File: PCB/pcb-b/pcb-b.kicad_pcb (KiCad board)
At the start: 2 copper layers, 90.3 x 40 mm, 82 parts, among them J1 Conn_02x05_Counter_Clockwise, J2 Conn_02x05_Counter_Clockwise, K1 HK19F-DCxxV-SHC, Q1 BC817, Q10 BC817, Q11 TPCA8120,L1Q, Q13 TPCA8120,L1Q, Q14 BC817, Q15 BC817, Q19 BC817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

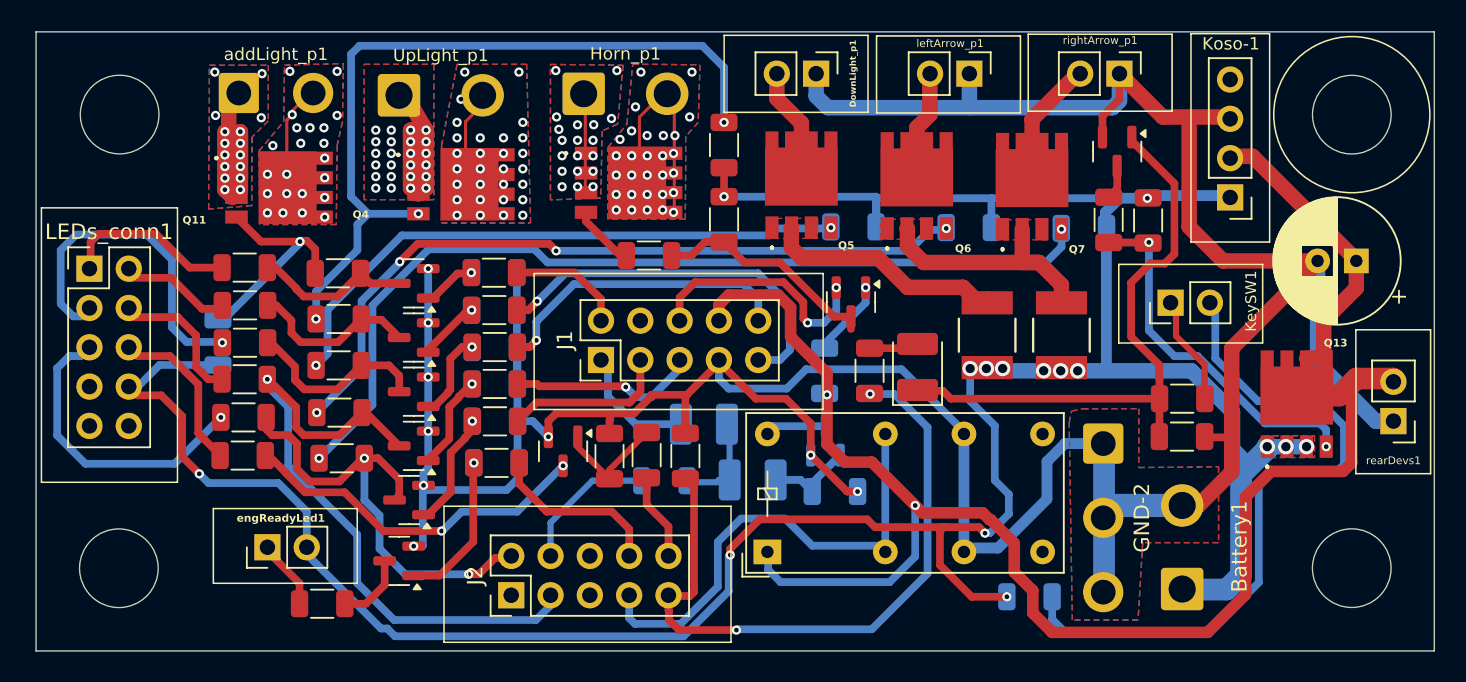
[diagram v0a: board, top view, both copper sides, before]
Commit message: PCB(b) size reduction and unuseful resistors removed
Originally, I placed resistors between the MOSFET's gate and the NPN collector to reduce the possible VGS voltage difference.
But, reading the TCPA8120's datasheet I have seen it accepts VGS max -20!! But in motorbike battey I never see 20 volts. So,
I removed the resistors. Now, when the NPN is conducing then the VGS will be about -12 volts, it is also better to avoid the
MOSFETs work in linear mode.

Thank to this component removing, also the PCB size has been reduced (85.6mm x 40.0mm). But, in order to get the size reduction
the add-light connector has been splitted in two single wite connectors. It is not beautiful to see, bet the PCB size is a too
big problem, and multilayer solution is a too expensive one!
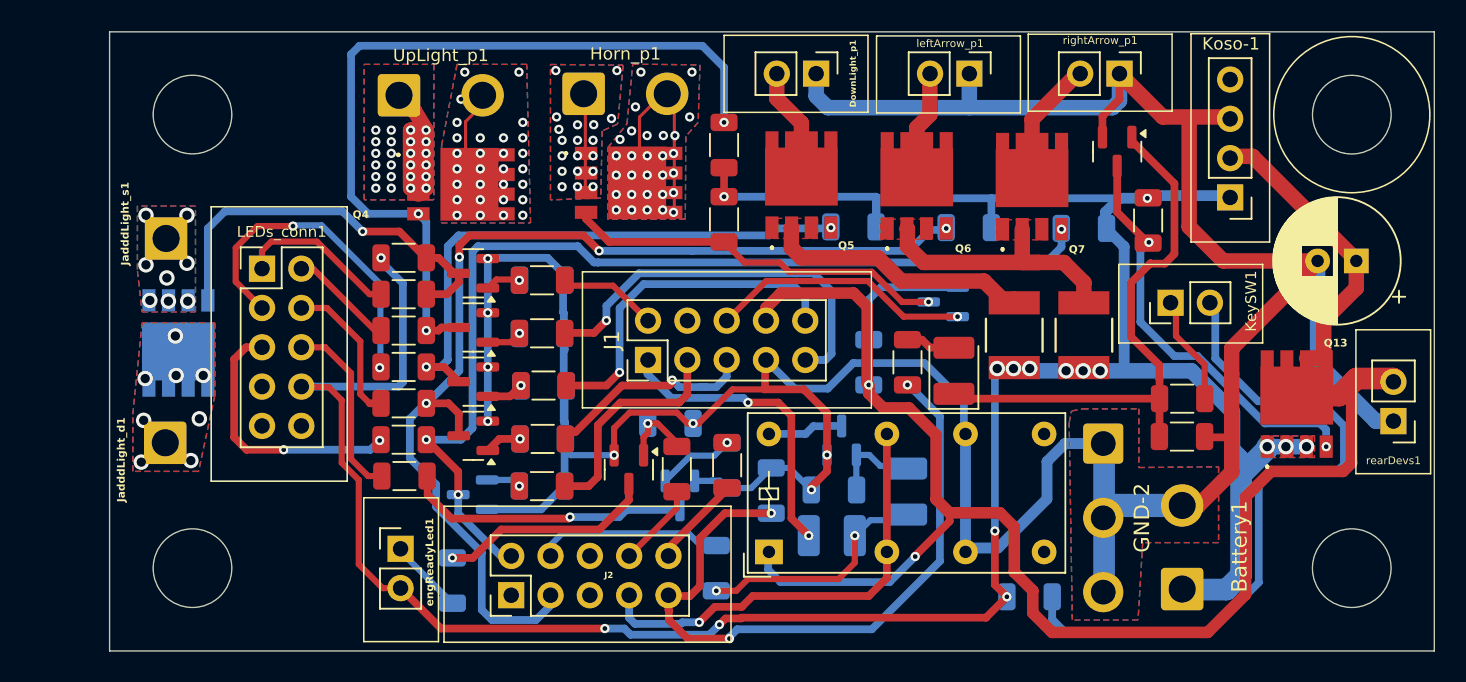
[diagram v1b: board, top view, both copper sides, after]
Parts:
- removed R3, RA10, RA11, RA12, RA13, RA14, RA7: 33K, Resistor_SMD:R_1206_3216Metric
- removed addLight_p1: Conn_01x02, Connector_Wire:SolderWire-0.75sqmm_1x02_P4.8mm_D1.25mm_OD2.3mm
- added JadddLight_d1: Conn_01x01, Connector_Wire:SolderWire-1sqmm_1x01_D1.4mm_OD2.7mm, F.Cu at (110.5, 96.5)
- added JadddLight_s1: Conn_01x01, Connector_Wire:SolderWire-1sqmm_1x01_D1.4mm_OD2.7mm, F.Cu at (110.5, 83.3)
- Q10, Q11, Q19, Q20, R6, RA39, RA9: moved to B.Cu
- R2, RA25, RA26, RA27, RA28: value 10K -> 15K
- RA24: value 10K -> 15K; moved to F.Cu
- RA42: value 10k -> 15k
- moved Q21 16.0 mm to (140.4, 98.3), turned to -90 degrees
- moved RA24 13.2 mm to (125.9, 84.6), turned to 0 degrees
- moved Q11 12.0 mm to (111.3, 90.1), turned to 0 degrees
- moved RA16 11.7 mm to (143.6, 98.2), turned to -90 degrees
- moved RA40 11.5 mm to (143.1, 95.3)
- moved LEDs_conn1 11.2 mm to (116.8, 85.3)
- moved D3 11.0 mm to (153.6, 102.5)
- moved RA6 10.5 mm to (126.0, 98.7)
- moved RA5 10.4 mm to (125.9, 96.3)
- moved RA1 10.4 mm to (125.9, 87.0)
- moved RA4 10.4 mm to (125.9, 94.0)
- moved RA2 10.4 mm to (125.9, 89.3)
- moved RA3 10.4 mm to (125.9, 91.7)
- moved D2 9.98 mm to (158.4, 99.7), turned to -90 degrees
- moved engReadyLed1 8.60 mm to (125.7, 103.4), turned to 0 degrees
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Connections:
- Q11 pad 4: Net-(Q11-G) -> Net-(Q1-C)
- Q4 pad 4: Net-(Q4-G) -> Net-(Q2-C)
- Q5 pad 4: Net-(Q5-G) -> Net-(Q14-C)
- Q6 pad 4: Net-(Q6-G) -> c_leftArrow
- Q7 pad 4: Net-(Q7-G) -> c_rightArrow
- Q8 pad 4: Net-(Q8-G) -> Net-(Q10-C)
- Q9 pad 3: Net-(Q9-C) -> Net-(Q13-G)
- RA24 pad 2: Net-(Q11-G) -> Net-(Q1-C)
- RA25 pad 2: Net-(Q4-G) -> Net-(Q2-C)
- RA26 pad 2: Net-(Q5-G) -> Net-(Q14-C)
- RA27 pad 2: Net-(Q6-G) -> c_leftArrow
- RA28 pad 2: Net-(Q7-G) -> c_rightArrow
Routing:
- net Net-(Q7-G): track 59.5 -> 0.00 mm, vias 2 -> 0
- net Net-(Q4-G): track 50.8 -> 0.00 mm, vias 3 -> 0
- net Net-(Q6-G): track 48.5 -> 0.00 mm, vias 4 -> 0
- net Net-(Q2-C): track 11.1 -> 52.4 mm, vias 0 -> 3
- net Net-(Q5-G): track 38.6 -> 0.00 mm, vias 2 -> 0
- net c_rightArrow: track 30.3 -> 65.4 mm, vias 2 -> 3
- net c_leftArrow: track 42.4 -> 69.2 mm, vias 1 -> 4
- net Net-(Q14-C): track 12.2 -> 36.7 mm, vias 0 -> 2
- net Net-(JadddLight_s1-Pin_1): track 16.7 -> 0.00 mm, vias 16 -> 8
- net Net-(Q1-C): track 10.2 -> 26.0 mm, vias 0 -> 1
- net Net-(Q11-G): track 15.0 -> 0.00 mm, vias 1 -> 0
- net i_powerOFF: track 7.99 -> 19.6 mm, vias 0 -> 2
- net Net-(Q10-C): track 14.7 -> 24.8 mm, vias 0 -> 1
- net Net-(Q21-C): track 4.63 -> 14.0 mm, vias 0 -> 1
- net Net-(D2-A): track 6.53 -> 15.4 mm, vias 0 -> 2
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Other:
- board size 90.3 x 40 mm -> 85.6 x 40 mm

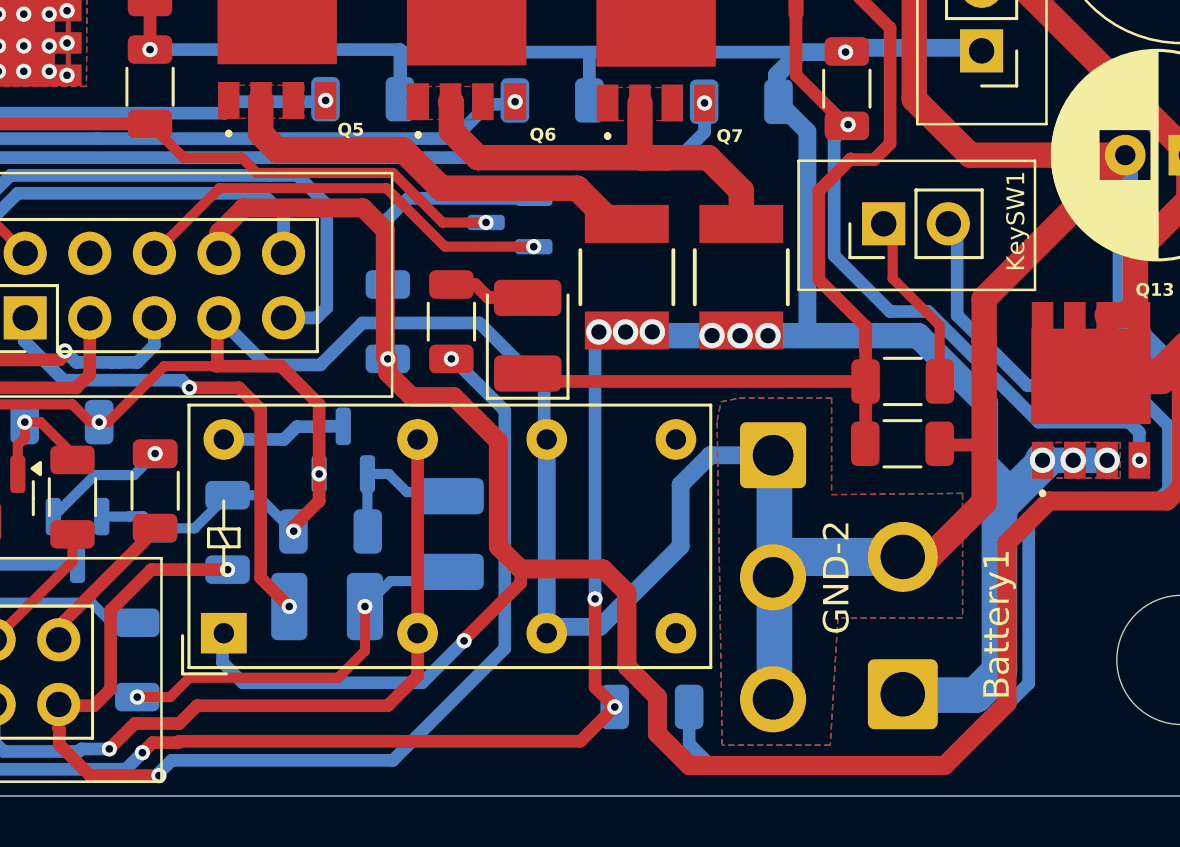
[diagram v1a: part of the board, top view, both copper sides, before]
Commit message: Flyback diode added
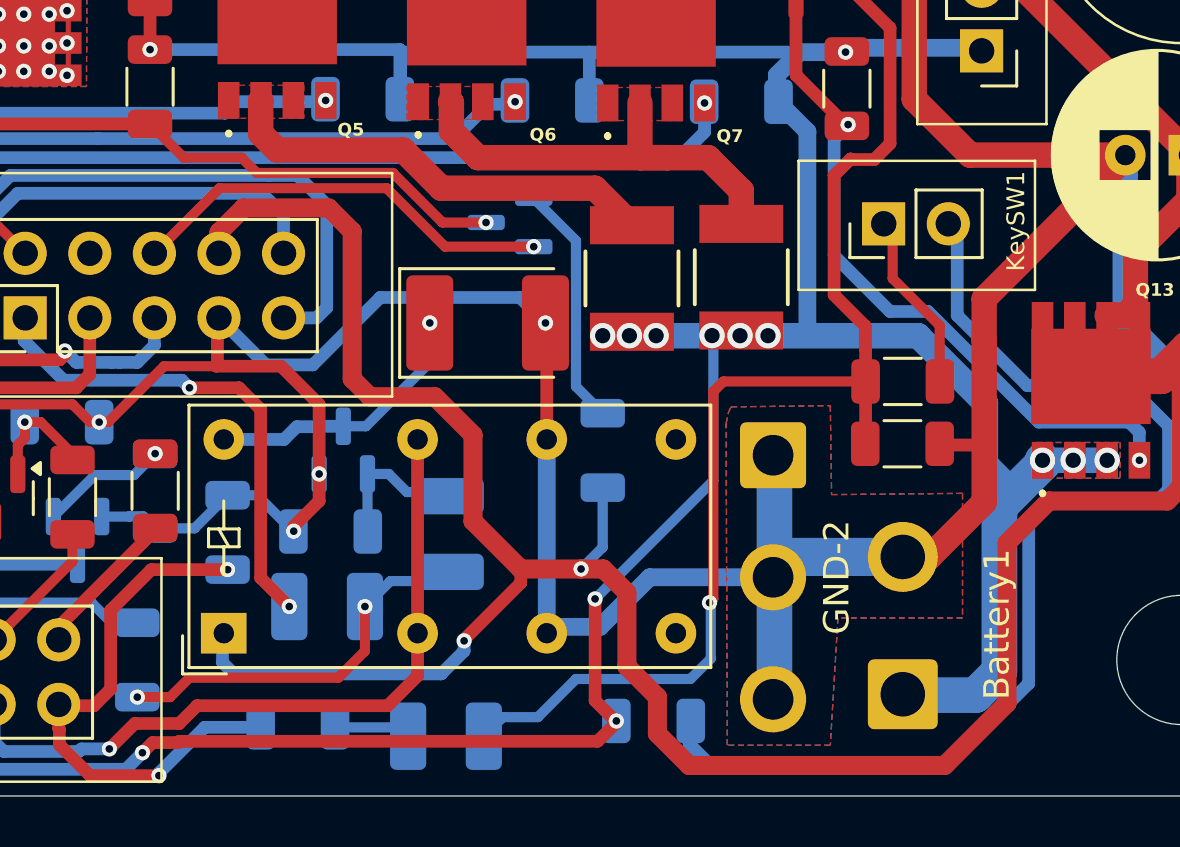
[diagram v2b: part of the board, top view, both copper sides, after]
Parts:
- added flyback-1: M7, Diode_SMD:D_2114_3652Metric_Pad1.85x3.75mm_HandSolder, F.Cu at (159.9, 91.4)
- D1, R5: moved to B.Cu
- moved R5 17.1 mm to (152.4, 107.3), turned to 180 degrees
- moved D1 16.1 mm to (158.2, 107.7), turned to 180 degrees
- moved RA23 9.85 mm to (164.4, 96.4)
- moved R1 0.55 mm to (166.4, 107.0)
- moved F1 0.21 mm to (165.6, 89.7)
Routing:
- net o_keepAlive: track 44.7 -> 21.6 mm, vias 3 -> 2
- net Net-(D1-K): track 36.4 -> 49.4 mm, vias 0 -> 1
- net Net-(Q3-C): track 4.91 -> 10.9 mm, vias 0 -> 1
- net tempPower: track 111.4 -> 114.6 mm
- net +12V: track 181.5 -> 182.6 mm
- net GND: track 223.0 -> 222.1 mm, vias 8 -> 9
- net Net-(Q10-B): track 8.66 -> 9.57 mm
- net Net-(KeySW1-Pin_2): track 45.2 -> 44.7 mm

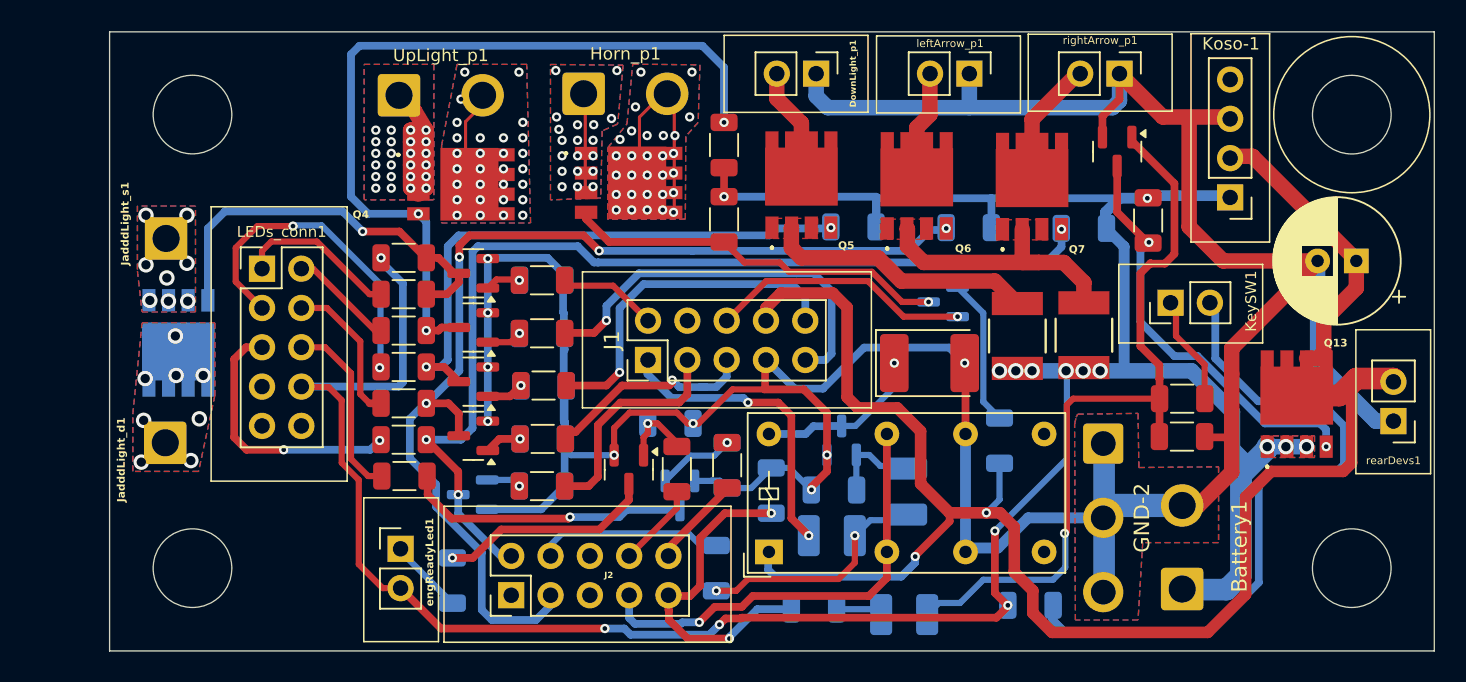
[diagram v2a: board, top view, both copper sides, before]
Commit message: Wrong PMEG40T30ER diode's footprint fixed
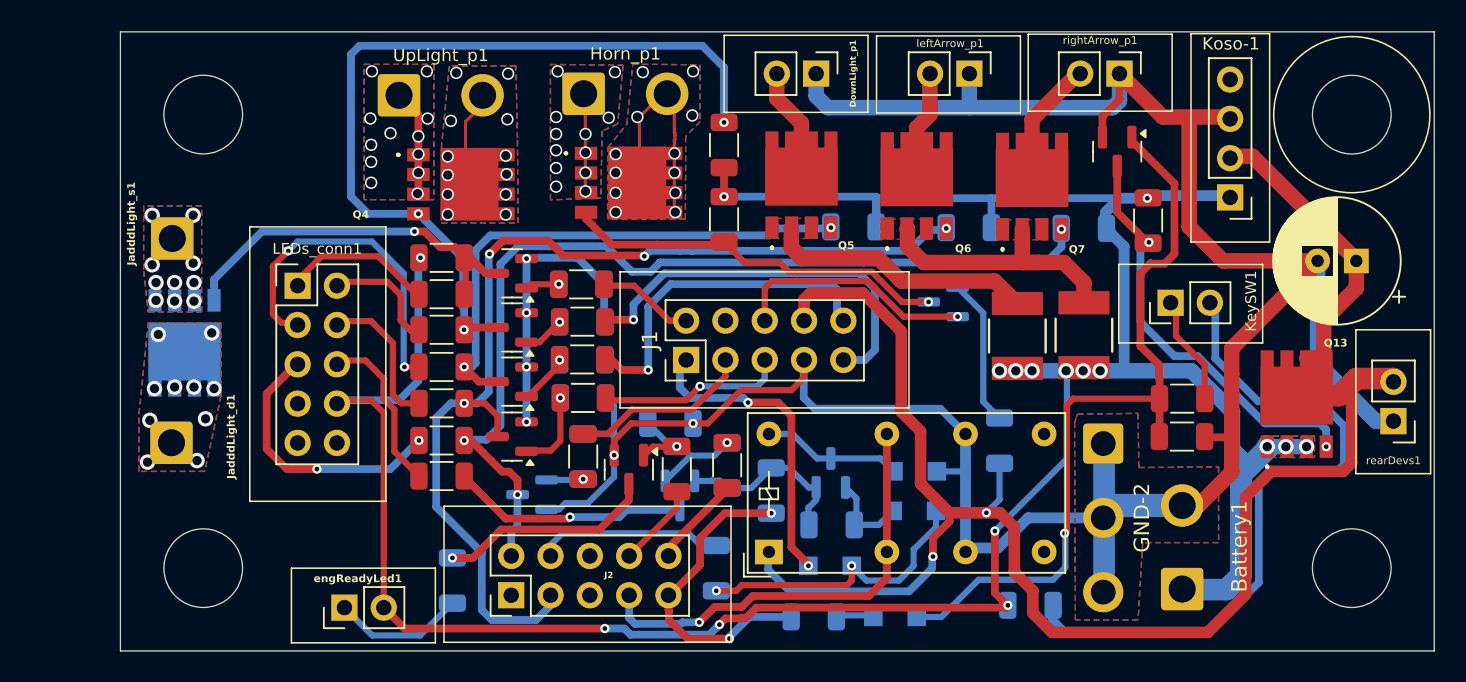
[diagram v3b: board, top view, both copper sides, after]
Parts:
- D1, D2, D3: value D_Small -> PMEG40T30ER; footprint Diode_SMD:D_1210_3225Metric_Pad1.42x2.65mm_HandSolder -> Diode_SMD:Nexperia_CFP3_SOD-123W
- flyback-1: value M7 -> PMEG40T30ER; footprint Diode_SMD:D_2114_3652Metric_Pad1.85x3.75mm_HandSolder -> Diode_SMD:Nexperia_CFP3_SOD-123W; moved to B.Cu
- moved flyback-1 7.06 mm to (158.9, 98.4)
- moved engReadyLed1 5.25 mm to (122.1, 107.2), turned to 90 degrees
- moved Q19 3.84 mm to (134.2, 99.9)
- moved RA19 3.71 mm to (137.5, 93.7)
- moved RA37 3.71 mm to (137.5, 93.7)
- moved RA18 3.28 mm to (137.5, 97.4), turned to 90 degrees
- moved RA38 3.26 mm to (137.5, 97.4), turned to 90 degrees
- moved RA36 3.01 mm to (137.4, 91.2)
- moved RA20 3.01 mm to (137.4, 91.2)
- moved RA21 2.71 mm to (137.4, 88.7)
- moved RA35 2.71 mm to (137.4, 88.8)
- moved LEDs_conn1 2.55 mm to (119.0, 86.4)
- moved RA22 2.55 mm to (137.4, 86.3)
- moved RA34 2.55 mm to (137.4, 86.3)
- moved Q15 2.50 mm to (132.9, 96.2)
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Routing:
- net GND: track 222.1 -> 199.9 mm, vias 9 -> 6
- net Net-(Q4-S_1): track 18.4 -> 9.61 mm, vias 24 -> 12
- net Net-(engReadyLed1-Pin_1): track 4.90 -> 8.59 mm
- net Net-(D2-A): track 15.4 -> 18.9 mm
- net c_rightArrow: track 65.4 -> 62.2 mm
- net Net-(Q20-C): track 18.4 -> 15.4 mm
- net o_rightArrow: track 14.6 -> 11.8 mm
- net +12V: track 182.6 -> 179.9 mm
- net Net-(Q14-C): track 36.7 -> 34.2 mm
- net Net-(Q15-B): track 3.03 -> 5.24 mm
- net c_leftArrow: track 69.2 -> 67.2 mm
- net Net-(Q3-C): track 10.9 -> 9.05 mm, vias 1 -> 0
- net Net-(LEDs_conn1-Pin_6): track 12.5 -> 10.9 mm
- net o_leftArrow: track 13.6 -> 12.1 mm
- net Net-(Q1-C): track 26.0 -> 24.6 mm
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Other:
- board size 85.6 x 40 mm -> 84.9 x 40 mm

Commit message: Floating FET's source pin fixed
The pin was in floating state when the associated external fuse is burnt
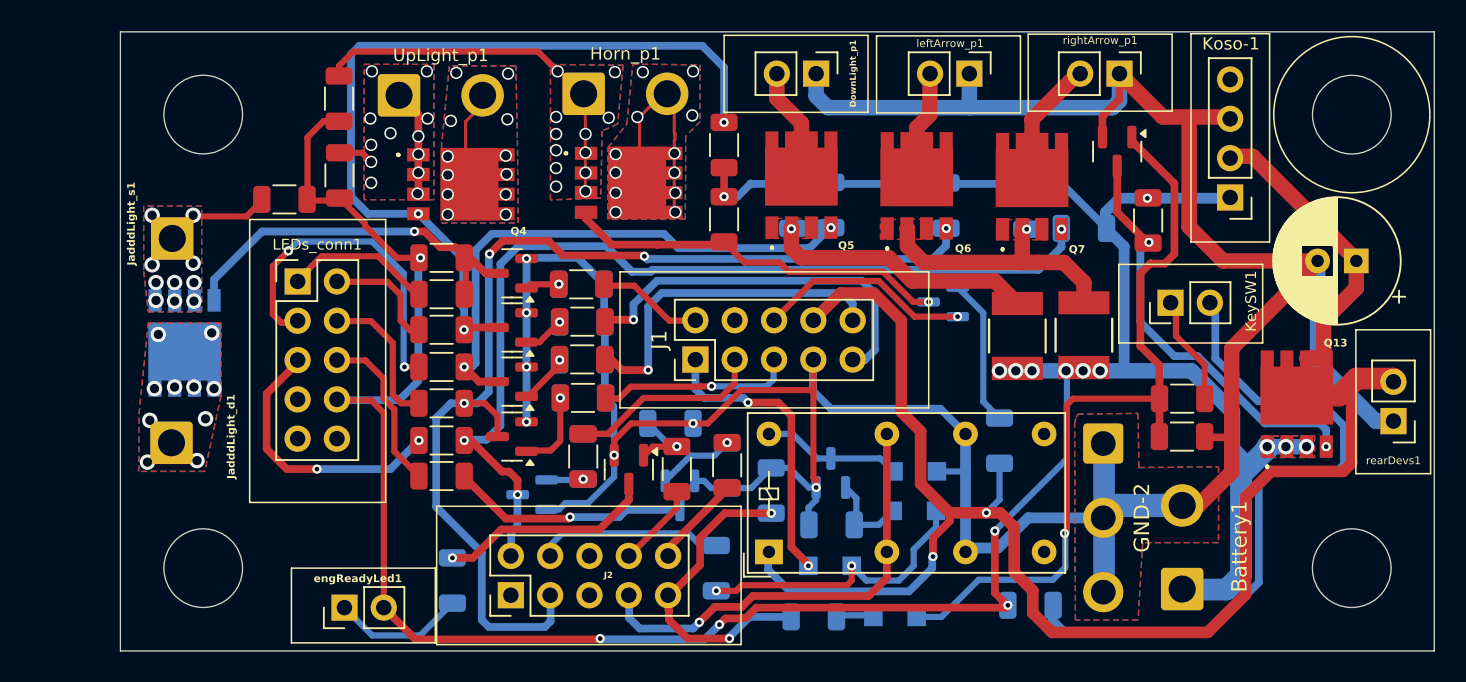
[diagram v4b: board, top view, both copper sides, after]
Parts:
- added RA10: 100K, Resistor_SMD:R_1206_3216Metric, F.Cu at (121.8, 79.3)
- added RA11: 100K, Resistor_SMD:R_1206_3216Metric, B.Cu at (151.0, 81.2)
- added RA12: 100K, Resistor_SMD:R_1206_3216Metric, B.Cu at (166.2, 81.3)
- added RA13: 100K, Resistor_SMD:R_1206_3216Metric, F.Cu at (121.7, 74.3)
- added RA7: 100K, Resistor_SMD:R_1206_3216Metric, F.Cu at (118.2, 80.8)
- moved RA27 2.04 mm to (160.9, 81.2), turned to -90 degrees
- moved RA26 2.03 mm to (153.5, 81.2), turned to -90 degrees
- moved J1 0.60 mm to (144.8, 91.2)
- moved LEDs_conn1 0.28 mm to (119.0, 86.1)
- turned F2 to -90 degrees
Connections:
- F2 pad 1: +12V -> Net-(Q6-S_1)
- F2 pad 2: Net-(Q6-S_1) -> +12V
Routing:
- net Net-(Horn_p1-Pin_1): track 6.56 -> 22.2 mm
- net GND: track 199.9 -> 211.5 mm, vias 6 -> 7
- net +12V: track 179.9 -> 188.8 mm
- net Net-(JadddLight_s1-Pin_1): track 0.00 -> 4.98 mm
- net Net-(Q4-S_1): track 9.61 -> 12.0 mm
- net c_leftArrow: track 67.2 -> 69.4 mm
- net c_horn: track 15.7 -> 13.9 mm
- net o_rightArrow: track 11.8 -> 13.3 mm
- net o_upLight: track 26.0 -> 24.8 mm
- net i_powerOFF: track 20.1 -> 19.0 mm
- net tempPower: track 113.8 -> 112.8 mm
- net Net-(Q14-C): track 34.2 -> 35.1 mm
- net o_addLight: track 6.29 -> 6.90 mm
- net o_leftArrow: track 12.1 -> 12.7 mm
- net Net-(Q5-S_1): vias 0 -> 1
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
